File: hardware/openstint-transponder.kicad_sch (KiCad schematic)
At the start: 38 parts, among them J1 V+, J2 V-, Q1 PMGD280UN, U1 ATtiny1616-M, U2 10 MHz, U3 SPX3819M5-L-3-3

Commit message: v2 transponder - initial commit
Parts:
- D1, Q1: JLCPCB_CORRECTION (none) -> 0; 0; 180
- U1, U3: JLCPCB_CORRECTION (none) -> 0; 0; 270
- U2: LCSC C2901558 -> C2831380
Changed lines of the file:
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@@
+			)
+		)
+		(property "JLCPCB_CORRECTION" "0; 0; 180"
+			(at 245.11 139.7 0)
+			(effects
+				(font
+					(size 1.27 1.27)
+				)
+				(hide yes)
 			)
 		)
@@
 			)
 		)
+		(property "JLCPCB_CORRECTION" "0; 0; 270"
+			(at 92.71 58.42 0)
+			(effects
+				(font
+					(size 1.27 1.27)
+				)
+				(hide yes)
+			)
+		)
 		(pin "21"
 		)
@@
 			)
 		)
+		(property "JLCPCB_CORRECTION" "0; 0; 270"
+			(at 250.19 43.18 0)
+			(effects
+				(font
+					(size 1.27 1.27)
+				)
+				(hide yes)
+			)
+		)
 		(pin "1"
 		)
@@
 			)
 		)
+		(property "JLCPCB_CORRECTION" "0; 0; 180"
+			(at 45.72 50.8 0)
+			(effects
+				(font
+					(size 1.27 1.27)
+				)
+				(hide yes)
+			)
+		)
 		(pin "2"
 		)
@@
 			)
 		)
-		(property "Datasheet" "https://jlcpcb.com/api/file/downloadByFileSystemAccessId/8590197686655098880"
+		(property "Datasheet" "https://jlcpcb.com/api/file/downloadByFileSystemAccessId/8613786702142062592"
 			(at 142.24 48.26 0)
 			(effects
@@
 			)
 		)
-		(property "LCSC" "C2901558"
+		(property "LCSC" "C2831380"
 			(at 142.24 48.26 0)
 			(effects
@@
 			(at 219.71 139.7 0)
 			(effects
+				(font
+					(size 1.27 1.27)
+				)
+				(hide yes)
+			)
+		)
+		(property "JLCPCB_CORRECTION" "0; 0; 180"
+			(at 219.71 139.7 0)
+			(effects

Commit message: spin v2
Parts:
- removed C10, C2: 100n, Capacitor_SMD:C_0402_1005Metric, symbol Device:C
- removed C11: 1n, Capacitor_SMD:C_0402_1005Metric, symbol Device:C
- removed TP2: TestPoint, TestPoint:TestPoint_Pad_D1.0mm, symbol Connector:TestPoint
- added R10, R11: 22, Resistor_SMD:R_0402_1005Metric, symbol Device:R
- added R8, R9: 10, Resistor_SMD:R_0402_1005Metric, symbol Device:R
- added TP5: VTG, TestPoint:TestPoint_Pad_D1.0mm, symbol Connector:TestPoint
- C13, C14: value 22p -> 33p; LCSC C1555 -> C1562
- C5: value 10n -> 100n; LCSC C15195 -> C1525
- C6: value 1n -> 1800p/C0G; LCSC C1523 -> C385028
- D1: JLCPCB_CORRECTION 0; 0; 180 -> 0; 0; 0
- R3, R4: value 22 -> 0; LCSC C25092 -> C17168
- TP1: value TestPoint -> UDPI
- TP3: value TestPoint -> VDDA
- TP4: value TestPoint -> GND
- U1: value ATtiny1616-M -> ATtiny816/1616; LCSC C507118 -> C2052778
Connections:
- net +3.3V: now also TP5.1
- net A+: now also R8.2; no longer Q1.6 (D)
- net A-: now also R9.2; no longer Q1.3 (D)
- net ANT+: now also U1.8 (PA7); no longer U1.5 (PA4)
- net ANT-: now also U1.5 (PA4); no longer U1.8 (PA7)
- net GND: now also R10.1, R11.1; no longer C13.1, C14.2
- net ~{BLINKY}: now also U1.10 (PB4); no longer U1.6 (PA5)
- net UART0TXD: no longer names the net of U1.20 (PA1)
- new net: C14.2, R11.2
- new net: C13.1, R10.2
- new net D+: Q1.6 (D), R8.1
- new net D-: Q1.3 (D), R9.1
- no-connect marks 13 -> 14
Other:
- note added: "ANT signal is created by XOR & XNOR an internal CLK/2 signal with UART-TxD"
- note added: "Note: avoid FH (Guangdong Fenghua) caps, too britte"
- note added: "Old firmware beware, BLILNKY moved from PA5 to PB4"
- note removed: "ANT signal is created by XOR & XNOR an internal CLK/2 signal with UART-TxD, TP2 helps debugging"
- moved on the sheet: AE1, C1, C13, C14, C15, C6, D1, L2, L3, R3, R4, R5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

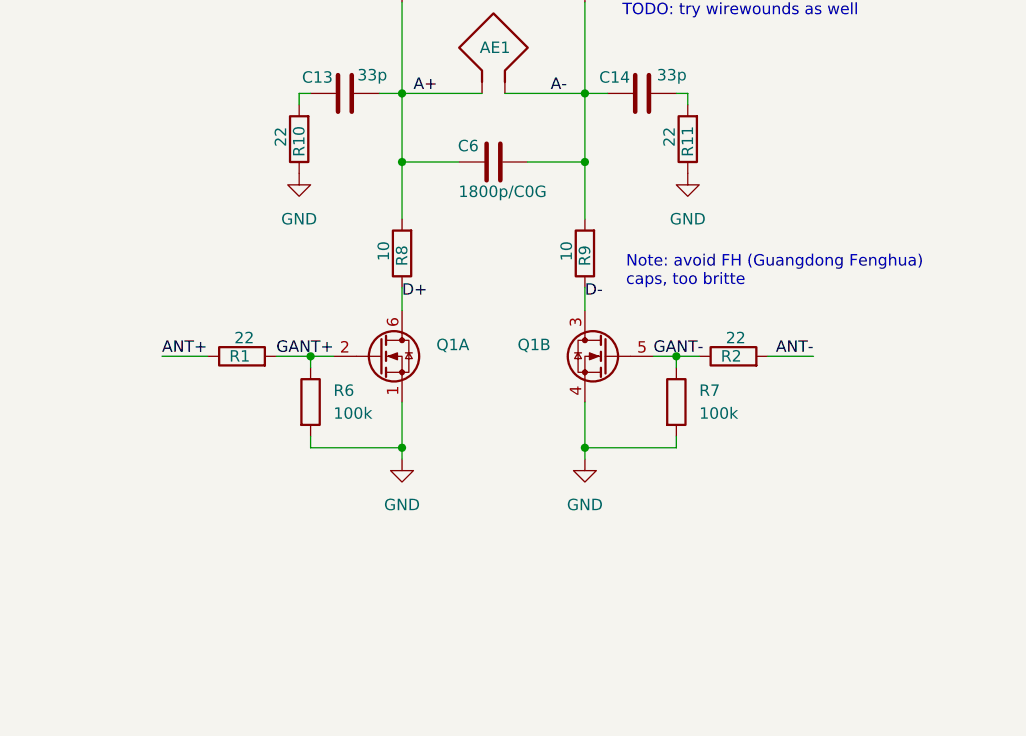
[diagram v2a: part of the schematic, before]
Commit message: use 2x tuning caps
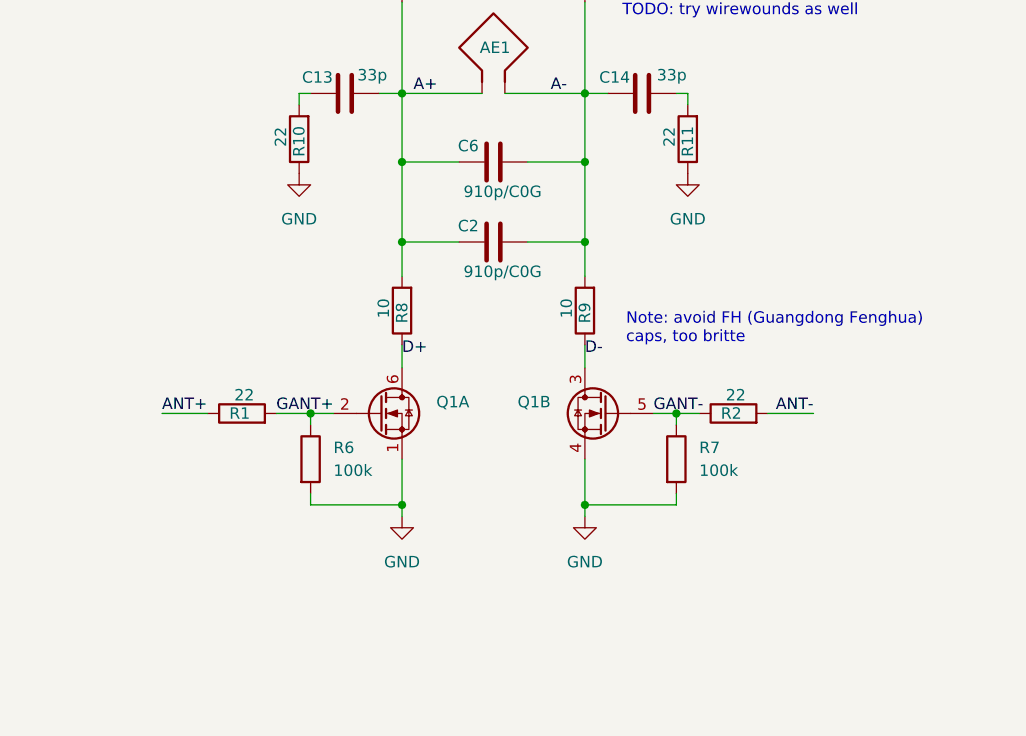
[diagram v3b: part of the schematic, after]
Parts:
- added C2: 910p/C0G, Capacitor_SMD:C_0402_1005Metric, symbol Device:C
- C6: value 1800p/C0G -> 910p/C0G; LCSC C385028 -> C2941944
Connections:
- net A+: now also C2.1
- net A-: now also C2.2
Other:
- moved on the sheet: Q1A, Q1B, R1, R2, R6, R7, R8, R9

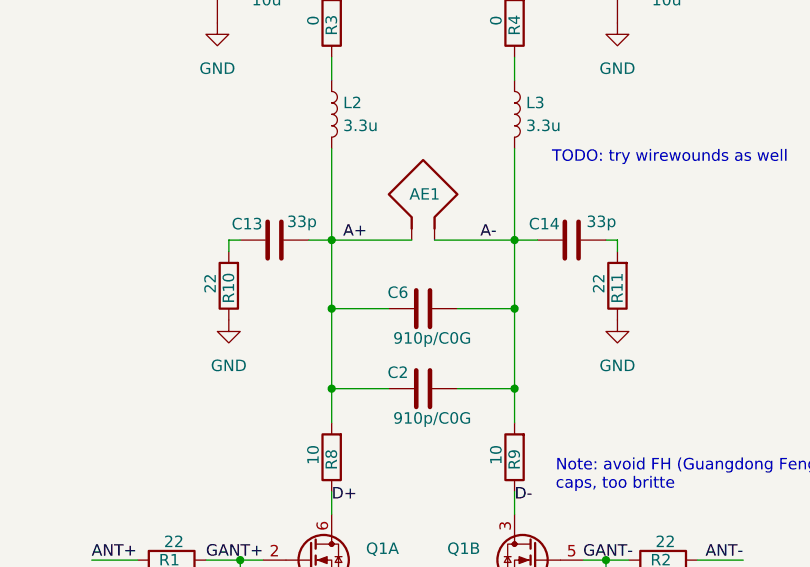
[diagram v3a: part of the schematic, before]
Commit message: fine-tune snubber values
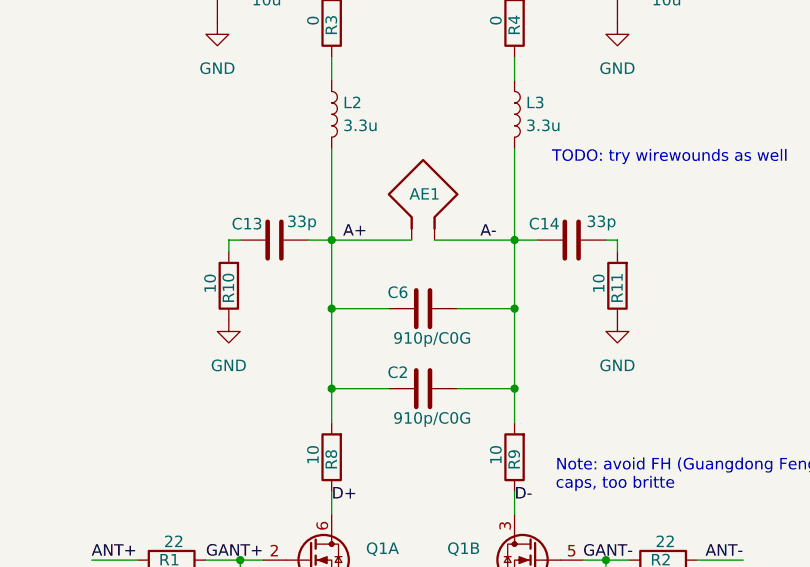
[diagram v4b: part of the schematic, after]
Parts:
- R10, R11: value 22 -> 10; LCSC C25092 -> C25077
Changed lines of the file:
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@@
 			)
 		)
-		(property "Value" "22"
+		(property "Value" "10"
 			(at 251.968 115.316 90)
 			(effects
@@
 			)
 		)
-		(property "LCSC" "C25092"
+		(property "LCSC" "C25077"
 			(at 254 115.57 90)
 			(effects
@@
 			)
 		)
-		(property "Value" "22"
+		(property "Value" "10"
 			(at 208.788 115.316 90)
 			(effects
@@
 			)
 		)
-		(property "LCSC" "C25092"
+		(property "LCSC" "C25077"
 			(at 210.82 115.57 90)
 			(effects
